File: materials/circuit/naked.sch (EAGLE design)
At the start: 17 parts, among them IC1 LM358N

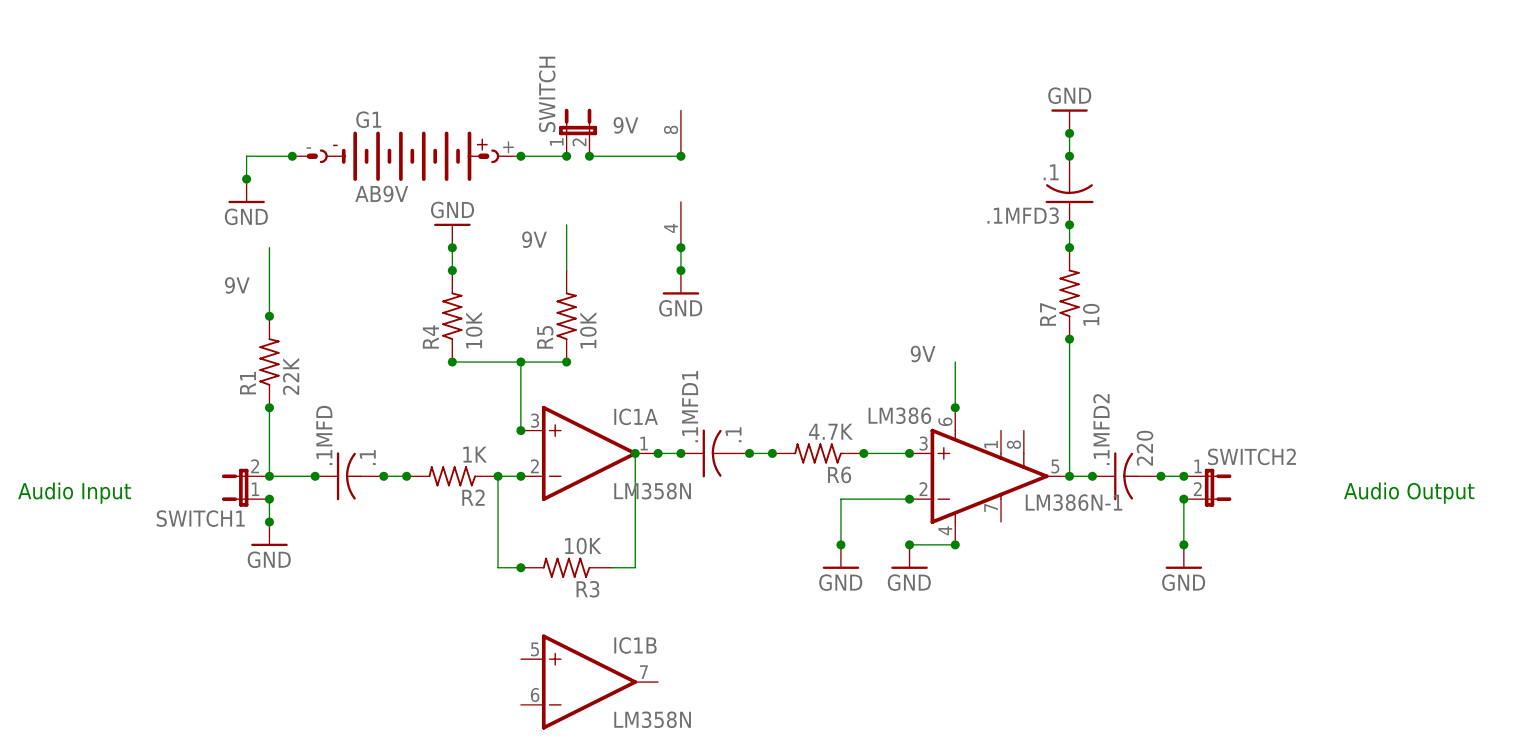
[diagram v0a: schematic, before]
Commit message: deleted brd, updated board w led and pot
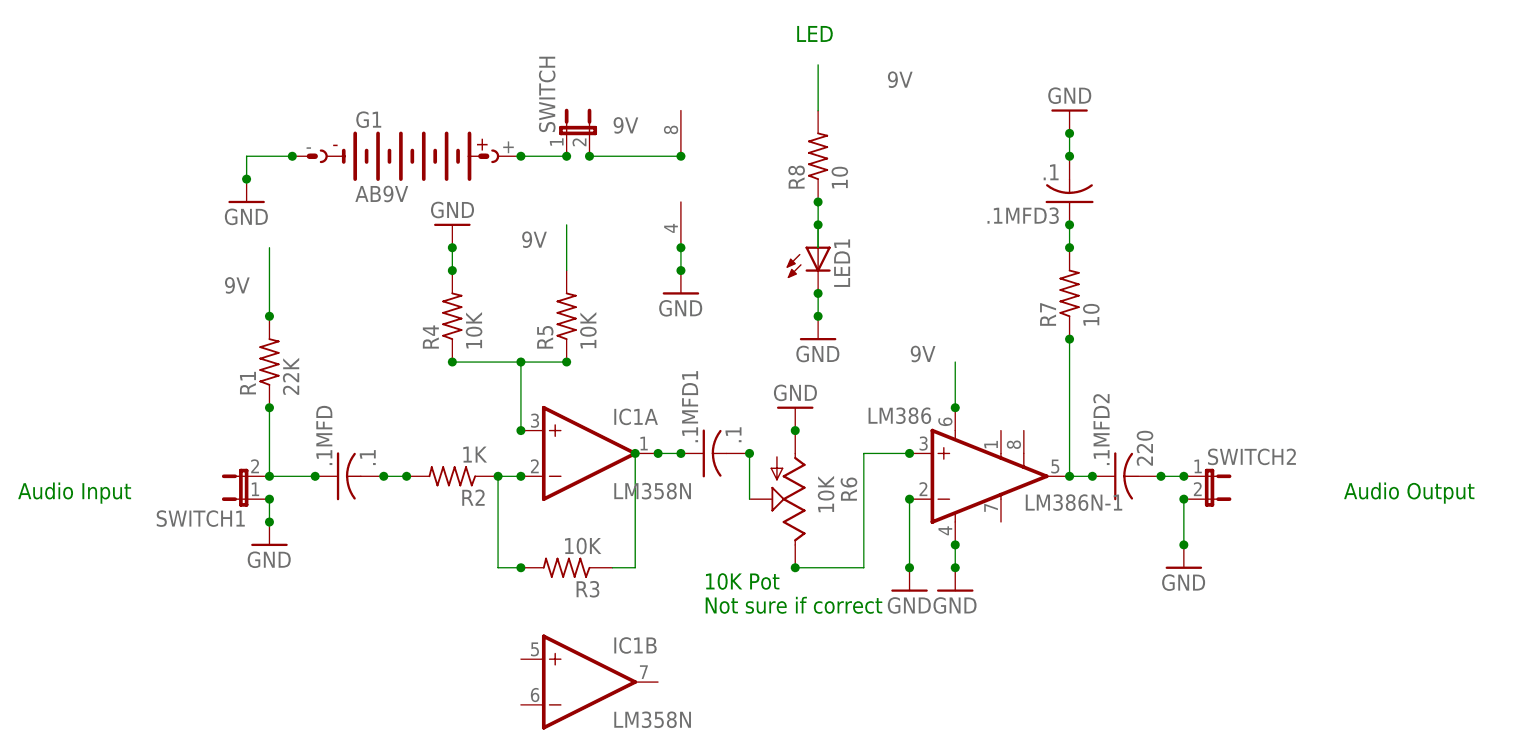
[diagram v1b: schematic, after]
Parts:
- added LED1: (no value), led:LED5MM
- added R8: 10, resistor:R-US_0204/7
- R6: value 4.7K -> 10K; device resistor:R-US_0204/7 -> pot:TRIM_US-PT10
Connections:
- new net N$12: LED1.A, R8.1
- net 9V: now also R8.2
- net GND: now also LED1.C, R6.A
- net N$8: now also R6.S; no longer R6.2
- net N$9: now also R6.E; no longer R6.1
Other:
- note added: "10K Pot Not sure if correct"
- note added: "LED"
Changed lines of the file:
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@@
 <part name="GND1" library="supply1" deviceset="GND" device=""/>
 <part name=".1MFD1" library="resistor" deviceset="C-US" device="025-024X044" value=".1"/>
-<part name="R6" library="resistor" deviceset="R-US_" device="0204/7" value="4.7K"/>
 <part name=".1MFD2" library="resistor" deviceset="C-US" device="025-024X044" value="220"/>
 <part name="SWITCH2" library="jumper" deviceset="JP1E" device=""/>
@@
 <part name=".1MFD3" library="resistor" deviceset="C-US" device="025-024X044" value=".1"/>
 <part name="GND8" library="supply1" deviceset="GND" device=""/>
+<part name="LED1" library="led" deviceset="LED" device="5MM"/>
+<part name="GND9" library="supply1" deviceset="GND" device=""/>
+<part name="R8" library="resistor" deviceset="R-US_" device="0204/7" value="10"/>
+<part name="R6" library="pot" deviceset="TRIM_US-" device="PT10" value="10K"/>
+<part name="GND10" library="supply1" deviceset="GND" device=""/>
 </parts>
 <sheets>
@@
 <text x="-27.94" y="55.88" size="1.778" layer="91">Audio Input</text>
 <text x="119.38" y="55.88" size="1.778" layer="91">Audio Output</text>
+<text x="58.42" y="106.68" size="1.778" layer="91">LED</text>
+<text x="48.26" y="43.18" size="1.778" layer="91">10K Pot
+Not sure if correct</text>
 </plain>
 <instances>
@@
 <instance part="IC1" gate="P" x="45.72" y="91.44"/>
 <instance part="GND2" gate="1" x="45.72" y="78.74"/>
-<instance part="GND3" gate="1" x="71.12" y="48.26"/>
-<instance part="GND4" gate="1" x="63.5" y="48.26"/>
+<instance part="GND3" gate="1" x="76.2" y="45.72"/>
+<instance part="GND4" gate="1" x="71.12" y="45.72"/>
 <instance part="G1" gate="G$1" x="15.24" y="93.98"/>
 <instance part="GND5" gate="1" x="-2.54" y="88.9"/>
@@
 <instance part="GND1" gate="1" x="20.32" y="86.36" rot="R180"/>
 <instance part=".1MFD1" gate="G$1" x="48.26" y="60.96" rot="R90"/>
-<instance part="R6" gate="G$1" x="60.96" y="60.96" rot="R180"/>
 <instance part=".1MFD2" gate="G$1" x="93.98" y="58.42" rot="R90"/>
 <instance part="SWITCH2" gate="A" x="104.14" y="58.42" rot="R270"/>
@@
 <instance part=".1MFD3" gate="G$1" x="88.9" y="88.9" rot="R180"/>
 <instance part="GND8" gate="1" x="88.9" y="99.06" rot="R180"/>
+<instance part="LED1" gate="G$1" x="60.96" y="83.82"/>
+<instance part="GND9" gate="1" x="60.96" y="73.66"/>
+<instance part="R8" gate="G$1" x="60.96" y="93.98" rot="R90"/>
+<instance part="R6" gate="G$1" x="58.42" y="55.88" rot="R180"/>
+<instance part="GND10" gate="1" x="58.42" y="66.04" rot="R180"/>
 </instances>
 <busses>
@@
 <pinref part="LM386" gate="G$1" pin="GND"/>
 <pinref part="GND3" gate="1" pin="GND"/>
-<wire x1="76.2" y1="50.8" x2="71.12" y2="50.8" width="0.1524" layer="91"/>
-<junction x="71.12" y="50.8"/>
+<wire x1="76.2" y1="50.8" x2="76.2" y2="48.26" width="0.1524" layer="91"/>
+<junction x="76.2" y="48.26"/>
 <junction x="76.2" y="50.8"/>
 </segment>
 <segment>
 <pinref part="GND4" gate="1" pin="GND"/>
-<wire x1="63.5" y1="50.8" x2="63.5" y2="55.88" width="0.1524" layer="91"/>
+<wire x1="71.12" y1="48.26" x2="71.12" y2="55.88" width="0.1524" layer="91"/>
 <pinref part="LM386" gate="G$1" pin="-IN"/>
-<wire x1="63.5" y1="55.88" x2="71.12" y2="55.88" width="0.1524" layer="91"/>
-<junction x="63.5" y="50.8"/>
+<junction x="71.12" y="48.26"/>
 <junction x="71.12" y="55.88"/>
 </segment>
@@
 <junction x="88.9" y="93.98"/>
 </segment>
+<segment>
+<pinref part="LED1" gate="G$1" pin="C"/>
+<pinref part="GND9" gate="1" pin="GND"/>
+<wire x1="60.96" y1="76.2" x2="60.96" y2="78.74" width="0.1524" layer="91"/>
+<junction x="60.96" y="78.74"/>
+<junction x="60.96" y="76.2"/>
+</segment>
+<segment>
+<pinref part="R6" gate="G$1" pin="A"/>
+<pinref part="GND10" gate="1" pin="GND"/>
+<junction x="58.42" y="63.5"/>
+</segment>
 </net>
 <net name="N$1" class="0">
@@
 <wire x1="33.02" y1="81.28" x2="33.02" y2="86.36" width="0.1524" layer="91"/>
 <label x="27.94" y="83.82" size="1.778" layer="95"/>
+</segment>
+<segment>
+<pinref part="R8" gate="G$1" pin="2"/>
+<wire x1="60.96" y1="99.06" x2="60.96" y2="104.14" width="0.1524" layer="91"/>
+<label x="68.58" y="101.6" size="1.778" layer="95"/>
 </segment>
 </net>
@@
 <segment>
 <pinref part=".1MFD1" gate="G$1" pin="2"/>
-<pinref part="R6" gate="G$1" pin="2"/>
-<wire x1="53.34" y1="60.96" x2="55.88" y2="60.96" width="0.1524" layer="91"/>
+<wire x1="53.34" y1="60.96" x2="53.34" y2="55.88" width="0.1524" layer="91"/>
 <junction x="53.34" y="60.96"/>
-<junction x="55.88" y="60.96"/>
+<pinref part="R6" gate="G$1" pin="S"/>
 </segment>
 </net>
 <net name="N$9" class="0">
 <segment>
-<pinref part="R6" gate="G$1" pin="1"/>
 <pinref part="LM386" gate="G$1" pin="+IN"/>
 <wire x1="66.04" y1="60.96" x2="71.12" y2="60.96" width="0.1524" layer="91"/>
-<junction x="66.04" y="60.96"/>
 <junction x="71.12" y="60.96"/>
+<pinref part="R6" gate="G$1" pin="E"/>
+<wire x1="58.42" y1="48.26" x2="66.04" y2="48.26" width="0.1524" layer="91"/>
+<wire x1="66.04" y1="48.26" x2="66.04" y2="60.96" width="0.1524" layer="91"/>
+<junction x="58.42" y="48.26"/>
 </segment>
 </net>
@@
 </segment>
 </net>
+<net name="N$12" class="0">
+<segment>
+<pinref part="R8" gate="G$1" pin="1"/>
+<wire x1="60.96" y1="88.9" x2="60.96" y2="86.36" width="0.1524" layer="91"/>
+<wire x1="60.96" y1="83.82" x2="60.96" y2="86.36" width="0.1524" layer="91"/>
+<pinref part="LED1" gate="G$1" pin="A"/>
+<junction x="60.96" y="86.36"/>
+<junction x="60.96" y="88.9"/>
+</segment>
+</net>
 </nets>
 </sheet>
@@
 </schematic>
 </drawing>
+<compatibility>
+<note version="6.3" minversion="6.2.2" severity="warning">
+Since Version 6.2.2 text objects can contain more than one line,
+which will not be processed correctly with this version.
+</note>
+</compatibility>
 </eagle>

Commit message: added box designs, circuit, presentation etc
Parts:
- removed .1MFD2: 220, resistor:C-US025-024X044
- removed R6: 10K, pot:TRIM_US-PT10
- added C3: 220uF, rcl:CPOL-USE3.5-8
- added C5: 10uF, resistor:C-US025-024X044
- added POT: 10k, jumper:JP2E
- C1, C2, C4: value .1 -> .1uF
- R8: value 10 -> 1k
- renumbered .1MFD to C1, .1MFD1 to C2, .1MFD3 to C4, SWITCH1 to IN, SWITCH2 to OUT
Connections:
- new net N$14: C5.2, LM386.GAIN@2
- net 9V: now also IC1P.V+
- net GND: now also POT.1; no longer R6.A
- net N$10: now also C3.+; no longer .1MFD2.1
- net N$11: now also C3.-; no longer .1MFD2.2
- net N$5: now also C5.1, LM386.GAIN@1; no longer R3.1
- net N$7: now also R3.1
- net N$8: now also POT.3; no longer R6.S
- net N$9: now also POT.2; no longer R6.E
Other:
- moved on the sheet: R3
